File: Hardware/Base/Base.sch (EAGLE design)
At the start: 24 parts, among them T1 2N3904, T2 2N3904, T3 2N3904, T4 2N3904, T5 2N3904

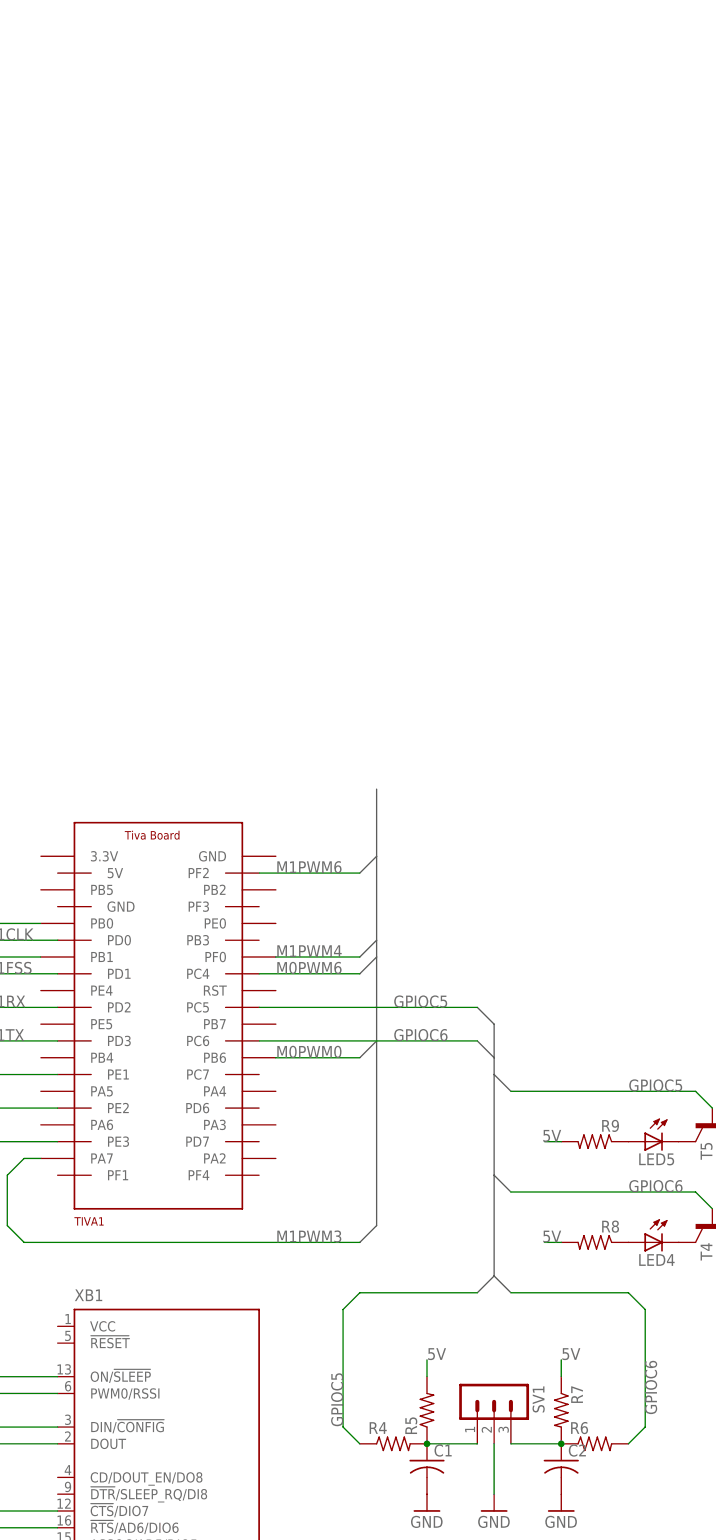
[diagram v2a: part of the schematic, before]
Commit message: Add servos to base schematic.
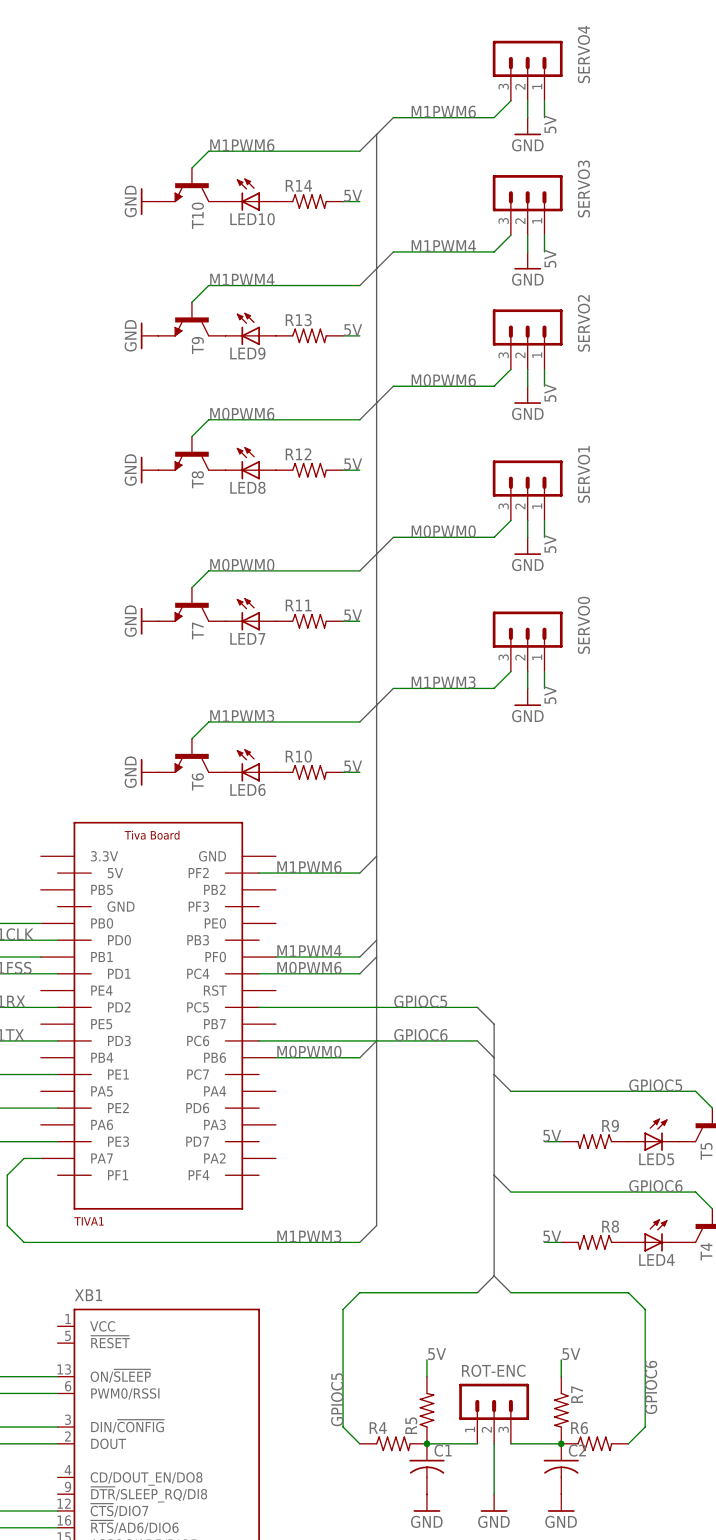
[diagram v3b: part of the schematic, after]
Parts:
- added LED10, LED6, LED7, LED8, LED9: (no value), led:LED5MM
- added R10, R11, R12, R13, R14: (no value), rcl:R-US_0207/7
- added SERVO0, SERVO1, SERVO2, SERVO3, SERVO4: (no value), con-lstb:MA03-1
- added T10, T6, T7, T8, T9: 2N3904, transistor:2N3904
- renumbered SV1 to ROT-ENC
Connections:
- new net N$13: LED6.C, T6.C
- new net N$14: LED6.A, R10.1
- new net N$15: LED7.C, T7.C
- new net N$16: LED7.A, R11.1
- new net N$17: LED8.C, T8.C
- new net N$18: LED8.A, R12.1
- new net N$19: LED9.C, T9.C
- new net N$20: LED9.A, R13.1
- new net N$21: LED10.C, T10.C
- new net N$22: LED10.A, R14.1
- net 5V: now also R10.2, R11.2, R12.2, R13.2, R14.2, SERVO0.1, SERVO1.1, SERVO2.1, SERVO3.1, SERVO4.1
- net GND: now also SERVO0.2, SERVO1.2, SERVO2.2, SERVO3.2, SERVO4.2, T10.E, T6.E, T7.E, T8.E, T9.E
- net M0PWM0: now also SERVO1.3, T7.B
- net M0PWM6: now also SERVO2.3, T8.B
- net M1PWM3: now also SERVO0.3, T6.B
- net M1PWM4: now also SERVO3.3, T9.B
- net M1PWM6: now also SERVO4.3, T10.B

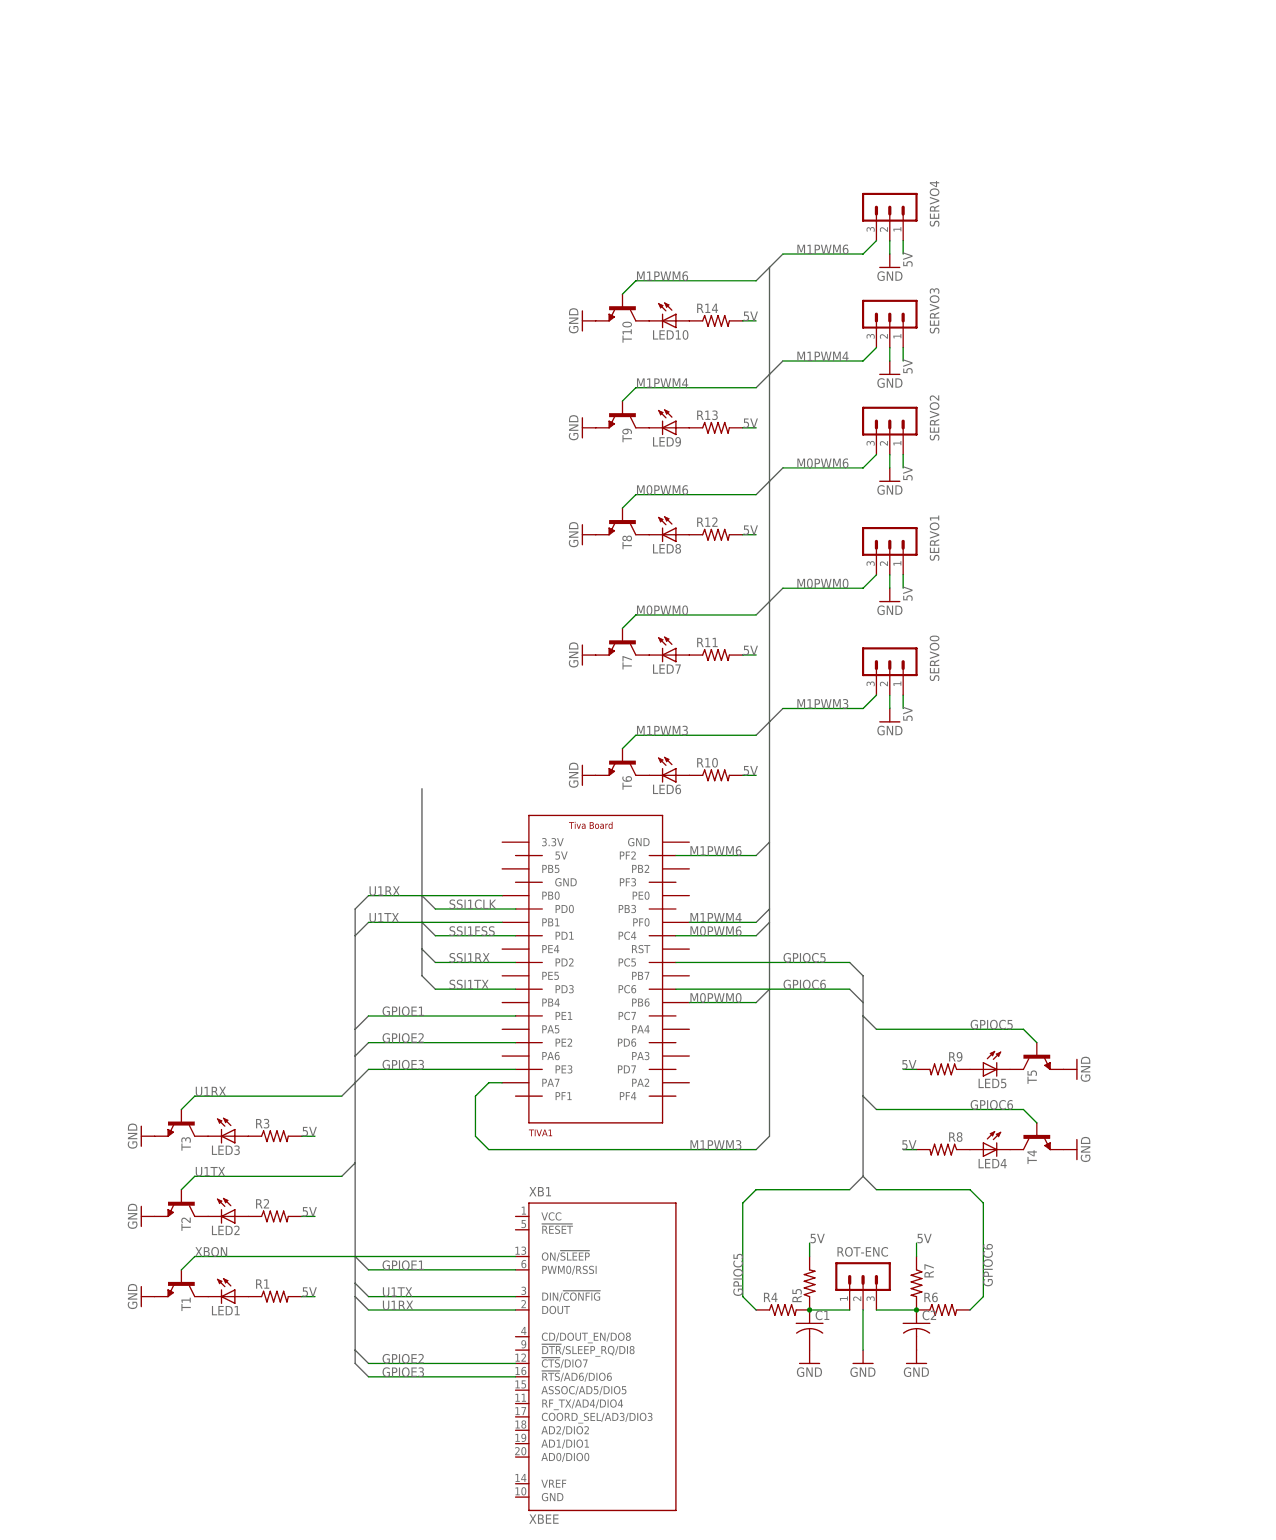
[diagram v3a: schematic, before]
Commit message: Added power supplies.
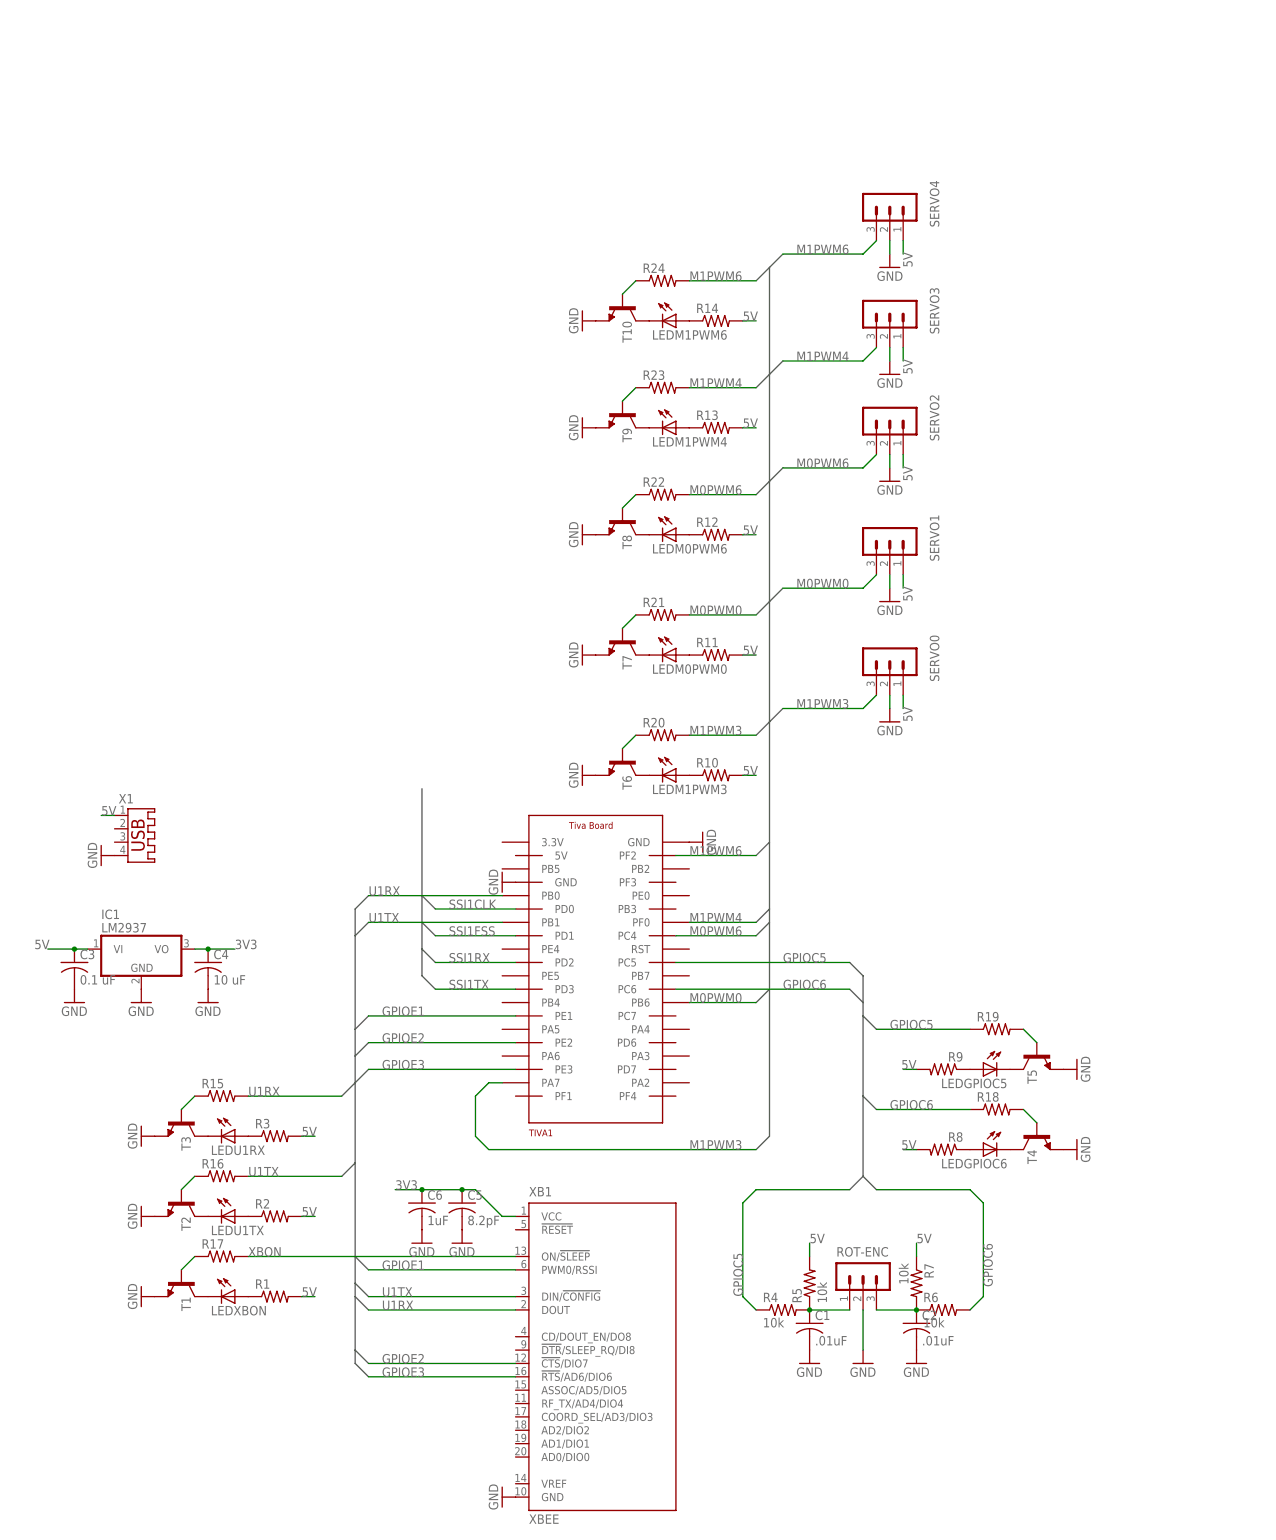
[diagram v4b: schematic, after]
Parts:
- added C3: 0.1 uF, rcl:C-US025-025X050
- added C4: 10 uF, rcl:C-US025-025X050
- added C5: 8.2pF, rcl:C-US025-025X050
- added C6: 1uF, rcl:C-US025-025X050
- added IC1: LM2937, linear:LM2937
- added R15, R16, R17, R18, R19, R20, R21, R22, R23, R24: (no value), rcl:R-US_0207/7
- added X1: (no value), con-yamaichi:USB-A003
- C1, C2: value (none) -> .01uF
- R4, R5, R6, R7: value (none) -> 10k
- renumbered LED1 to LEDXBON, LED10 to LEDM1PWM6, LED2 to LEDU1TX, LED3 to LEDU1RX, LED4 to LEDGPIOC6, LED5 to LEDGPIOC5, LED6 to LEDM1PWM3, LED7 to LEDM0PWM0, LED8 to LEDM0PWM6, LED9 to LEDM1PWM4
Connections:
- new net 3V3: C4.1, C5.1, C6.1, IC1.VO, XB1.VCC
- new net N$23: R24.1, T10.B
- new net N$24: R23.1, T9.B
- new net N$25: R22.1, T8.B
- new net N$26: R21.1, T7.B
- new net N$27: R20.1, T6.B
- new net N$28: R15.1, T3.B
- new net N$29: R16.1, T2.B
- new net N$30: R17.1, T1.B
- new net N$31: R18.2, T4.B
- new net N$32: R19.2, T5.B
- net 5V: now also C3.1, IC1.VI, X1.1
- net GND: now also C3.2, C4.2, C5.2, C6.2, IC1.GND, TIVA1.GND@1, TIVA1.GND@2, X1.4, XB1.GND
- net GPIOC5: now also R19.1; no longer T5.B
- net GPIOC6: now also R18.1; no longer T4.B
- net M0PWM0: now also R21.2; no longer T7.B
- net M0PWM6: now also R22.2; no longer T8.B
- net M1PWM3: now also R20.2; no longer T6.B
- net M1PWM4: now also R23.2; no longer T9.B
- net M1PWM6: now also R24.2; no longer T10.B
- net U1RX: now also R15.2; no longer T3.B
- net U1TX: now also R16.2; no longer T2.B
- net XBON: now also R17.2; no longer T1.B

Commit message: Finished rev0 base schematic.
Created board file.
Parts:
- added LCD: (no value), con-lstb:MA03-1
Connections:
- removed net SSI1CLK: TIVA1.PD0
- removed net SSI1FSS: TIVA1.PD1
- removed net SSI1RX: TIVA1.PD2
- removed net SSI1TX: TIVA1.PD3
- new net GPIOE5: LCD.1, TIVA1.PE5
- net 3V3: now also LCD.2
- net GND: now also LCD.3
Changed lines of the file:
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@@
 <part name="GND27" library="supply1" deviceset="GND" device=""/>
 <part name="GND25" library="supply1" deviceset="GND" device=""/>
+<part name="LCD" library="con-lstb" deviceset="MA03-1" device=""/>
+<part name="GND28" library="supply1" deviceset="GND" device=""/>
 </parts>
 <sheets>
@@
 <instance part="GND27" gate="1" x="-5.08" y="45.72" rot="R270"/>
 <instance part="GND25" gate="1" x="-5.08" y="-71.12" rot="R270"/>
+<instance part="LCD" gate="G$1" x="-12.7" y="96.52" smashed="yes" rot="MR270">
+<attribute name="VALUE" x="-5.08" y="97.79" size="1.778" layer="96" rot="MR270"/>
+<attribute name="NAME" x="-5.08" y="91.44" size="1.778" layer="95" rot="MR90"/>
+</instance>
+<instance part="GND28" gate="1" x="-15.24" y="83.82"/>
 </instances>
 <busses>
-<bus name="SSI1CLK,SSI1FSS,SSI1RX,SSI1TX">
-<segment>
-<wire x1="-17.78" y1="25.4" x2="-20.32" y2="27.94" width="0.762" layer="92"/>
-<wire x1="-20.32" y1="27.94" x2="-20.32" y2="33.02" width="0.762" layer="92"/>
-<wire x1="-20.32" y1="33.02" x2="-20.32" y2="38.1" width="0.762" layer="92"/>
-<wire x1="-20.32" y1="38.1" x2="-20.32" y2="43.18" width="0.762" layer="92"/>
-<wire x1="-20.32" y1="43.18" x2="-20.32" y2="63.5" width="0.762" layer="92"/>
-<wire x1="-20.32" y1="33.02" x2="-17.78" y2="30.48" width="0.762" layer="92"/>
-<wire x1="-20.32" y1="38.1" x2="-17.78" y2="35.56" width="0.762" layer="92"/>
-<wire x1="-20.32" y1="43.18" x2="-17.78" y2="40.64" width="0.762" layer="92"/>
-</segment>
-</bus>
 <bus name="U1RX,U1TX,GPIOE1,GPIOE2,GPIOE3">
 <segment>
@@
 </busses>
 <nets>
-<net name="SSI1CLK" class="0">
-<segment>
-<pinref part="TIVA1" gate="TIVA" pin="PD0"/>
-<wire x1="-2.54" y1="40.64" x2="-17.78" y2="40.64" width="0.1524" layer="91"/>
-<label x="-15.24" y="40.64" size="1.778" layer="95"/>
-</segment>
-</net>
-<net name="SSI1FSS" class="0">
-<segment>
-<pinref part="TIVA1" gate="TIVA" pin="PD1"/>
-<wire x1="-17.78" y1="35.56" x2="-2.54" y2="35.56" width="0.1524" layer="91"/>
-<label x="-15.24" y="35.56" size="1.778" layer="95"/>
-</segment>
-</net>
-<net name="SSI1RX" class="0">
-<segment>
-<pinref part="TIVA1" gate="TIVA" pin="PD2"/>
-<wire x1="-17.78" y1="30.48" x2="-2.54" y2="30.48" width="0.1524" layer="91"/>
-<label x="-15.24" y="30.48" size="1.778" layer="95"/>
-</segment>
-</net>
-<net name="SSI1TX" class="0">
-<segment>
-<pinref part="TIVA1" gate="TIVA" pin="PD3"/>
-<wire x1="-17.78" y1="25.4" x2="-2.54" y2="25.4" width="0.1524" layer="91"/>
-<label x="-15.24" y="25.4" size="1.778" layer="95"/>
-</segment>
-</net>
 <net name="U1RX" class="0">
 <segment>
@@
 <pinref part="XB1" gate="G$1" pin="GND"/>
 <pinref part="GND25" gate="1" pin="GND"/>
+</segment>
+<segment>
+<pinref part="LCD" gate="G$1" pin="3"/>
+<pinref part="GND28" gate="1" pin="GND"/>
+<wire x1="-15.24" y1="86.36" x2="-15.24" y2="88.9" width="0.1524" layer="91"/>
 </segment>
 </net>
@@
 <label x="-25.4" y="-12.7" size="1.778" layer="95"/>
 </segment>
+<segment>
+<pinref part="LCD" gate="G$1" pin="2"/>
+<wire x1="-12.7" y1="88.9" x2="-12.7" y2="86.36" width="0.1524" layer="91"/>
+<label x="-12.7" y="86.36" size="1.778" layer="95" rot="R90"/>
+</segment>
 </net>
 <net name="N$23" class="0">
@@
 </segment>
 </net>
+<net name="GPIOE5" class="0">
+<segment>
+<pinref part="TIVA1" gate="TIVA" pin="PE5"/>
+<wire x1="-5.08" y1="27.94" x2="-7.62" y2="27.94" width="0.1524" layer="91"/>
+<wire x1="-7.62" y1="27.94" x2="-10.16" y2="30.48" width="0.1524" layer="91"/>
+<wire x1="-10.16" y1="30.48" x2="-10.16" y2="88.9" width="0.1524" layer="91"/>
+<pinref part="LCD" gate="G$1" pin="1"/>
+<label x="-7.62" y="78.74" size="1.778" layer="95" rot="R90"/>
+</segment>
+</net>

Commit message: Lay out components of base PCB rev0.
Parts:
- removed C1, C2: .01uF, rcl:C-US025-025X050
- removed IC1: LM2937, linear:LM2937
- removed R4, R5, R6, R7: 10k, rcl:R-US_0207/7
- removed ROT-ENC: (no value), con-lstb:MA03-1
- added C7, C8, C9: .01uF, rcl:C-US025-025X050
- added LEDGPIOC7: (no value), led:LED5MM
- added R25, R26: (no value), rcl:R-US_0207/7
- added R27, R28, R29, R30, R31, R32: 10k, rcl:R-US_0207/7
- added REG3V3: 7806T, linear:7806T
- added ROTENC: (no value), con-lstb:MA05-1
- added SWITCH: (no value), pinhead:PINHD-1X2
- added T11: 2N3904, transistor:2N3904
- X1: device con-yamaichi:USB-A003 -> con-berg:PN87520
- renumbered TIVA1 to TIVA
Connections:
- removed net N$8: C2.1, R6.1, R7.2, ROT-ENC.3
- new net GPIOC7: R26.1, R30.1, TIVA.PC7
- new net N$33: LEDGPIOC7.C, T11.C
- new net N$34: LEDGPIOC7.A, R25.1
- new net N$35: R26.2, T11.B
- new net N$36: C7.1, R27.1, R30.2, ROTENC.4
- new net N$37: C8.1, R28.1, R32.2, ROTENC.3
- new net N$38: C9.1, R29.1, R31.2, ROTENC.2
- net 3V3: now also LCD.3, REG3V3.VO; no longer IC1.VO, LCD.2
- net 5V: now also R25.2, R27.2, R28.2, R29.2, REG3V3.VI, SWITCH.2; no longer IC1.VI, R5.2, R7.1, X1.1
- net GND: now also C7.2, C8.2, C9.2, LCD.2, REG3V3.GND, ROTENC.1, ROTENC.5, T11.E; no longer C1.2, C2.2, IC1.GND, LCD.3, ROT-ENC.2
- net GPIOC5: now also R31.1; no longer R4.1
- net GPIOC6: now also R32.1; no longer R6.2
- net N$7: now also SWITCH.1, X1.1; no longer C1.1, R4.2, R5.1, ROT-ENC.1
